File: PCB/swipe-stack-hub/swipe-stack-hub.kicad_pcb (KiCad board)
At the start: 2 copper layers, 59 parts, among them J1 Barrel_Jack_Switch, J2 Conn_02x08_Odd_Even, J3 Conn_02x05_Odd_Even, J4 Conn_01x06, J5 Conn_01x04, J6 Conn_01x01_Socket, J7 Conn_01x01_Socket, J8 Conn_01x01_Socket, J9 Conn_01x01_Socket, SW4 SW_Push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

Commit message: Justin's version of hub PCB
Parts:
- added LS1: Speaker, 477:Speaker, F.Cu at (153.4, 147.3)
- C10, C5, C7, C8, C9, R8: moved to B.Cu
- U3, U4: footprint hm:HM-11-MODULE -> 477:HM-11-MODULE
- moved J6 175.9 mm to (156.5, 109.7), turned to -90 degrees
- moved J7 172.4 mm to (151.9, 109.7), turned to -90 degrees
- moved J8 169.2 mm to (147.3, 109.7), turned to -90 degrees
- moved J9 166.3 mm to (142.7, 109.7), turned to -90 degrees
- moved R8 131.7 mm to (125.5, 112.5), turned to -90 degrees
- moved SW4 131.4 mm to (99.5, 122.1)
- moved SW5 131.4 mm to (99.5, 129.9)
- moved C7 128.3 mm to (142.2, 115.3), turned to -90 degrees
- moved C5 126.6 mm to (136.1, 131.3)
- moved C8 116.6 mm to (128.5, 108.8)
- moved C9 113.8 mm to (128.5, 129.5), turned to 180 degrees
- moved R7 112.2 mm to (107.7, 124.5), turned to 180 degrees
- moved R10 111.8 mm to (107.2, 132.1), turned to 180 degrees
- moved J5 110.7 mm to (170.2, 152.5), turned to 90 degrees
- moved C10 108.9 mm to (121.9, 120.4), turned to 90 degrees
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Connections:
- J2 pad 5: /PB3 -> /PB1
- U1 pad 27: /G0 -> /PB1
- U1 pad 28: /B0 -> /G0
- U1 pad 55: /PB3 -> /G1
- U1 pad 56: /G1 -> /B0
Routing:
- net +3.3V: track 286.4 -> 88.5 mm, vias 4 -> 6
- net /BLNK: track 183.0 -> 48.6 mm, vias 2 -> 0
- net /PB3: track 108.6 -> 0.00 mm, vias 2 -> 0
- net GND: track 74.3 -> 173.4 mm, vias 7 -> 25
- net /G1: track 133.6 -> 39.3 mm, vias 4 -> 0
- net /LAT: track 133.6 -> 40.8 mm, vias 2 -> 0
- net /A1: track 117.5 -> 27.5 mm, vias 2 -> 0
- net /A3: track 113.4 -> 28.1 mm, vias 2 -> 0
- net /A4: track 107.1 -> 30.8 mm, vias 2 -> 0
- net /G0: track 103.5 -> 31.7 mm, vias 2 -> 0
- net /A2: track 103.8 -> 35.9 mm, vias 2 -> 0
- net /NSS: track 0.00 -> 63.3 mm, vias 0 -> 2
- net /A0: track 105.6 -> 42.6 mm, vias 2 -> 0
- net /B1: track 110.5 -> 50.8 mm
- net /PA1: track 104.4 -> 45.2 mm, vias 2 -> 0
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- removed copper zone on F.Cu, net GND
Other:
- board outline added: 89.4 x 71.4 mm

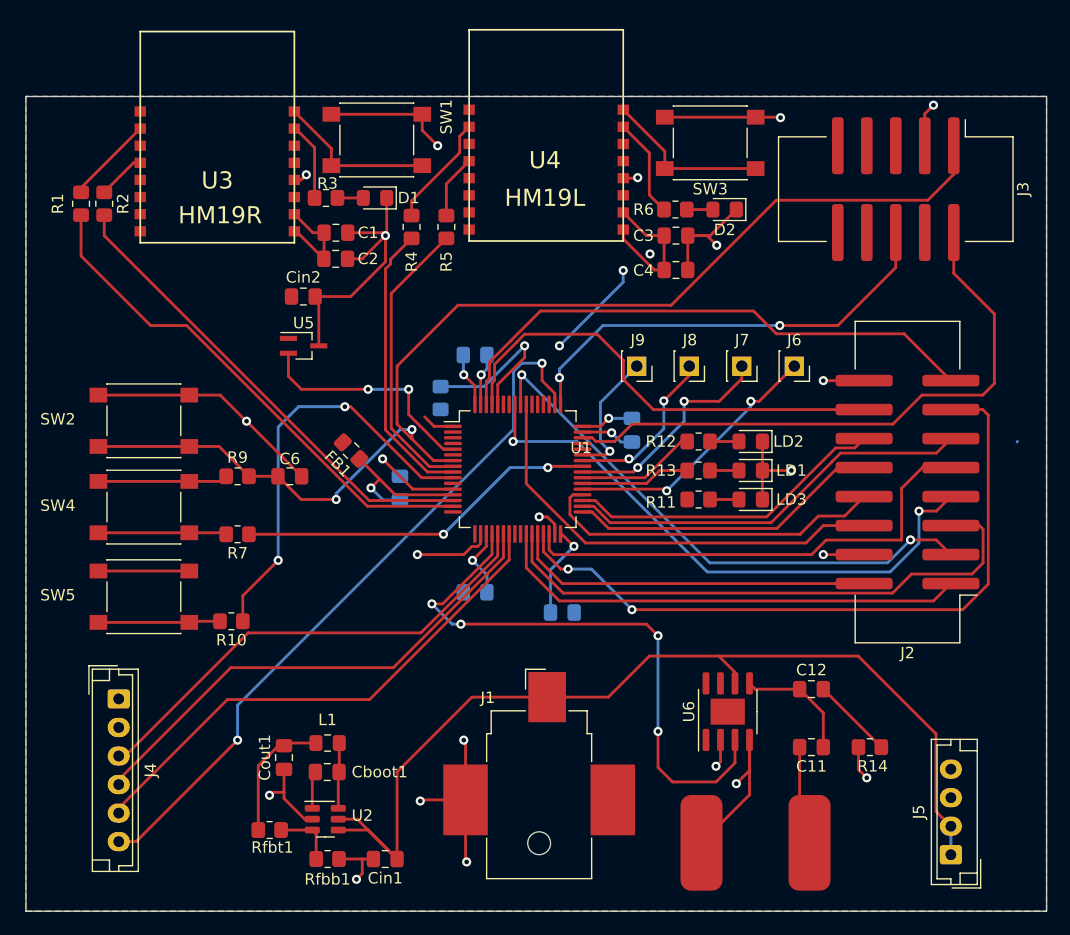
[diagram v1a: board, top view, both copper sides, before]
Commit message: changed some capacitors
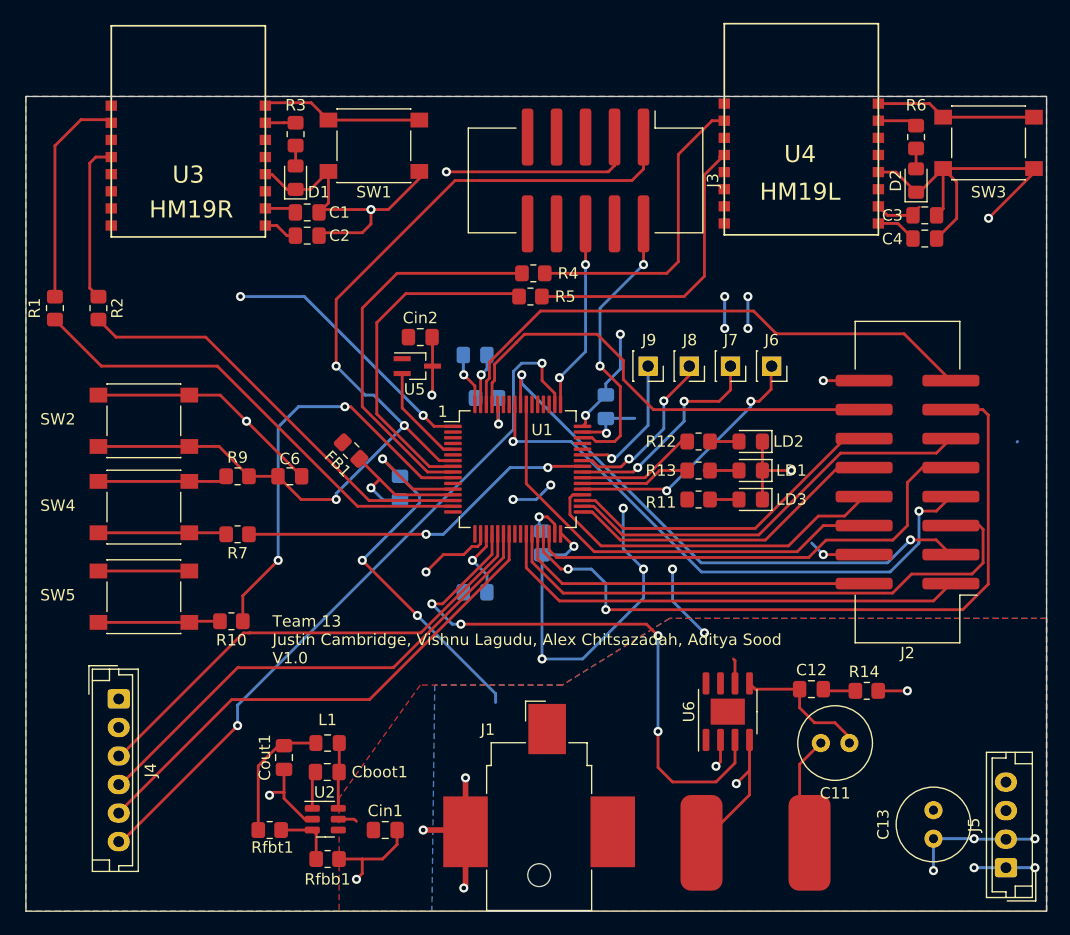
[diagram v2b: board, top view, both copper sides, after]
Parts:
- added C13: C_Small, Capacitor_THT:C_Radial_D6.3mm_H11.0mm_P2.50mm, F.Cu at (168.7, 151.1)
- C11: footprint Capacitor_SMD:C_0805_2012Metric_Pad1.18x1.45mm_HandSolder -> Capacitor_THT:C_Radial_D6.3mm_H7.0mm_P2.50mm
- moved J3 27.2 mm to (138.2, 93.5)
- moved SW3 24.4 mm to (173.5, 90.2), turned to 0 degrees
- moved U4 22.4 mm to (157.1, 89.5)
- moved R6 22.0 mm to (167.1, 89.7), turned to -90 degrees
- moved C4 22.0 mm to (167.9, 98.6)
- moved C3 21.9 mm to (167.9, 96.5)
- moved D2 17.0 mm to (167.1, 93.5), turned to 90 degrees
- moved R4 11.4 mm to (133.6, 101.6), turned to 180 degrees
- moved Cin2 10.8 mm to (123.7, 107.2)
- moved U5 10.1 mm to (123.4, 109.7)
- moved R5 9.56 mm to (133.3, 103.6), turned to 180 degrees
- moved R1 9.43 mm to (91.7, 104.6)
- moved R2 9.16 mm to (95.5, 104.6)
- moved D1 7.18 mm to (112.8, 93.2), turned to 90 degrees
- moved C5 6.35 mm to (134.4, 125.2), turned to 90 degrees
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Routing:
- net +5V: track 88.8 -> 20.9 mm, vias 0 -> 5
- net GND: track 173.4 -> 227.6 mm, vias 25 -> 23
- net +3.3V: track 88.5 -> 138.1 mm, vias 6 -> 18
- net /PA13: track 53.0 -> 24.5 mm, vias 0 -> 2
- net /PA14: track 39.4 -> 16.8 mm
- net Net-(U4-UART_RX): track 6.03 -> 26.8 mm
- net Net-(U4-UART_TX): track 9.86 -> 26.8 mm
- net /NRST: track 102.6 -> 85.7 mm, vias 2 -> 3
- net Net-(U3-UART_TX): track 7.73 -> 19.2 mm
- net /PF0: track 20.4 -> 8.96 mm, vias 2 -> 0
- net /BOOT0: track 15.0 -> 4.05 mm
- net Net-(U3-UART_RX): track 4.24 -> 14.1 mm
- net /PC1: track 25.2 -> 34.2 mm
- net Net-(U4-PIO1): track 8.72 -> 3.48 mm
- net /PC0: track 25.4 -> 30.1 mm
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- added copper zone on F.Cu, net +5V
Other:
- board text added: "1"
- board text added: "Team 13 Justin Cambridge, Vishnu Lagudu, Alex Chitsazadah, Aditya Sood V1.0"

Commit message: pcb changes
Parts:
- added RN1: R_Pack08, Library:SOIC127P762X240-16N, F.Cu at (183.2, 119.4)
- added RN2: R_Pack08, Library:SOIC127P762X240-16N, F.Cu at (158.0, 119.9)
- C11: footprint Capacitor_THT:C_Radial_D6.3mm_H7.0mm_P2.50mm -> Capacitor_THT:CP_Radial_D14.0mm_P7.50mm
- C13: footprint Capacitor_THT:C_Radial_D6.3mm_H11.0mm_P2.50mm -> Capacitor_THT:CP_Radial_D14.0mm_P5.00mm
- Cin2: value 2.2uF -> 0.1uF
- Cout1: footprint Capacitor_SMD:C_0805_2012Metric_Pad1.18x1.45mm_HandSolder -> Capacitor_THT:CP_Radial_D5.0mm_P2.50mm
- J3: footprint Connector_IDC:IDC-Header_2x05_P2.54mm_Vertical_SMD -> Connector_IDC:IDC-Header_2x05_P2.54mm_Vertical
- J4: footprint Connector_JST:JST_EH_B6B-EH-A_1x06_P2.50mm_Vertical -> Connector_JST:JST_VH_B6P-VH-B_1x06_P3.96mm_Vertical
- J5: footprint Connector_JST:JST_EH_B4B-EH-A_1x04_P2.50mm_Vertical -> Connector_JST:JST_VH_B4P-VH-B_1x04_P3.96mm_Vertical
- moved LD3 19.3 mm to (161.8, 104.4)
- moved R13 19.3 mm to (157.2, 104.4)
- moved LD1 19.1 mm to (161.8, 102.1)
- moved LD2 19.1 mm to (161.8, 99.6)
- moved R11 19.1 mm to (157.2, 102.1)
- moved R12 19.1 mm to (157.2, 99.6)
- moved C13 18.1 mm to (182.6, 139.7), turned to 180 degrees
- moved C6 11.5 mm to (103.9, 111.5), turned to -90 degrees
- moved J5 10.2 mm to (185.2, 153.2), turned to 180 degrees
- moved R14 8.98 mm to (154.7, 142.0), turned to 90 degrees
- moved R7 6.14 mm to (102.9, 120.7)
- moved R10 5.92 mm to (102.6, 128.3)
- moved SW2 5.84 mm to (95.2, 110.5)
- moved SW5 5.79 mm to (95.2, 126.0)
- moved C11 5.76 mm to (165.1, 138.4), turned to -90 degrees
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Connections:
- J2 pad 1: /PB0 -> Net-(J2-Pin_1)
- J2 pad 10: /A1 -> Net-(J2-Pin_10)
- J2 pad 11: /A2 -> Net-(J2-Pin_11)
- J2 pad 12: /A3 -> Net-(J2-Pin_12)
- J2 pad 13: /Clk -> Net-(J2-Pin_13)
- J2 pad 14: /LAT -> Net-(J2-Pin_14)
- J2 pad 15: /BLNK -> Net-(J2-Pin_15)
- J2 pad 16: GND -> Net-(J2-Pin_16)
- J2 pad 2: /G0 -> Net-(J2-Pin_2)
- J2 pad 3: /B0 -> Net-(J2-Pin_3)
- J2 pad 4: GND -> Net-(J2-Pin_4)
- J2 pad 5: /PB1 -> Net-(J2-Pin_5)
- J2 pad 6: /G1 -> Net-(J2-Pin_6)
- J2 pad 7: /B1 -> Net-(J2-Pin_7)
- J2 pad 8: /A4 -> Net-(J2-Pin_8)
- J2 pad 9: /A0 -> Net-(J2-Pin_9)
- U1 pad 27: /PB1 -> /G0
- U1 pad 28: /G0 -> /B0
- U1 pad 55: /G1 -> /PB3
- U1 pad 56: /B0 -> /G1
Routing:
- net /PB1: track 50.1 -> 0.00 mm
- net (no net): track 0.00 -> 50.1 mm
- net /PB3: track 0.00 -> 40.4 mm
- net /G0: track 31.7 -> 0.00 mm
- net /B0: track 48.9 -> 31.7 mm, vias 2 -> 0
- net +5V: track 20.9 -> 3.86 mm, vias 5 -> 0
- net GND: track 227.6 -> 210.8 mm, vias 23 -> 20
- net /A2: track 36.8 -> 26.4 mm
- net /NRST: track 85.7 -> 95.5 mm
- net /G1: track 40.0 -> 48.1 mm, vias 0 -> 2
- net /LAT: track 40.8 -> 34.0 mm
- net /PA8: track 31.7 -> 38.1 mm
- net /Clk: track 63.2 -> 69.6 mm
- net /BLNK: track 48.6 -> 53.4 mm
- net /MOSI: track 45.7 -> 50.4 mm
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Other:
- board size 89.4 x 71.4 mm -> 98.8 x 71.4 mm
- board text added: "Team 13 Justin Cambridge, Vishnu Lagudu, Alex Chitsazzadeh, Aditya Sood V1.0"
- board text removed: "Team 13 Justin Cambridge, Vishnu Lagudu, Alex Chitsazadah, Aditya Sood V1.0"

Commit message: uhhhhhh
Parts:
- moved Rfbb1 8.74 mm to (106.9, 151.6), turned to -90 degrees
- moved Rfbt1 6.29 mm to (104.6, 148.1), turned to -90 degrees
- moved Cout1 4.58 mm to (107.2, 144.8), turned to 90 degrees
- moved Cboot1 3.54 mm to (112.0, 145.0)
- moved Cin1 3.29 mm to (117.3, 150.1), turned to -90 degrees
- moved RN1 2.90 mm to (180.3, 119.9)
- moved J2 2.80 mm to (168.4, 119.9)
- moved U2 2.70 mm to (112.9, 148.3)
- moved L1 1.61 mm to (115.1, 144.3), turned to 90 degrees
- moved RN2 1.52 mm to (156.5, 119.9)
- moved LD2 0.25 mm to (161.8, 99.8)
- moved R12 0.25 mm to (157.2, 99.8)
- moved J5 0.25 mm to (184.9, 153.2)
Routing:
- net (no net): track 50.1 -> 0.00 mm
- net /G0: track 0.00 -> 30.6 mm, vias 0 -> 2
- net /B0: track 31.7 -> 56.4 mm, vias 0 -> 2
- net /PB3: track 40.4 -> 63.9 mm, vias 0 -> 2
- net /A2: track 26.4 -> 49.4 mm, vias 0 -> 2
- net /PC8: track 10.5 -> 32.5 mm, vias 0 -> 2
- net /PC7: track 9.64 -> 31.3 mm, vias 0 -> 2
- net /G1: track 48.1 -> 30.6 mm
- net /B1: track 50.9 -> 67.5 mm
- net /PB0: track 42.0 -> 57.5 mm
- net /A0: track 41.2 -> 56.1 mm, vias 0 -> 2
- net /A1: track 30.4 -> 19.3 mm
- net /A3: track 26.9 -> 16.5 mm
- net /BLNK: track 53.4 -> 63.7 mm
- net /A4: track 31.8 -> 22.2 mm
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- added copper zone on F.Cu, net GND
- added copper zone on F.Cu, net Net-(U2-SW)

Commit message: pcb ready for presentation
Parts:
- moved R5 2.30 mm to (133.6, 101.3)
- moved Cin2 2.29 mm to (123.7, 104.9)
- moved R4 2.29 mm to (133.6, 99.3)
- moved U5 2.29 mm to (123.4, 107.4)
- moved C10 2.06 mm to (123.7, 119.4)
- moved R9 0.81 mm to (103.4, 115.2)
- moved C6 0.57 mm to (103.4, 111.3)
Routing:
- net GND: track 206.9 -> 162.1 mm, vias 24 -> 31
- net +3.3V: track 136.8 -> 98.8 mm, vias 15 -> 12
- net /NSS: track 73.0 -> 67.0 mm
- net /NRST: track 94.9 -> 100.3 mm, vias 3 -> 5
- net /PC0: track 30.1 -> 34.0 mm
- net +5V: track 7.65 -> 10.7 mm
- net /G1: track 30.6 -> 27.7 mm
- net Net-(U4-UART_RX): track 26.8 -> 24.0 mm
- net Net-(U4-UART_TX): track 26.8 -> 24.0 mm
- net /PC1: track 34.2 -> 36.6 mm
- net /PF0: track 8.96 -> 11.2 mm
- net /PC2: track 38.6 -> 36.6 mm
- net /PA1: track 45.2 -> 47.1 mm, vias 0 -> 2
- net /PA0: track 41.9 -> 43.6 mm, vias 0 -> 2
- net /B0: track 56.4 -> 55.3 mm
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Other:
- outline, holes or cut-outs redrawn
- board text added: "swipe-stack HUB V1.0 Team 13: Justin Cambridge, Vishnu Lagudu, Alex Chitsazzadeh, Aditya Sood"
- board text removed: "Team 13 Justin Cambridge, Vishnu Lagudu, Alex Chitsazzadeh, Aditya Sood V1.0"
